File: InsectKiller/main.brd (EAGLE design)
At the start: 28 parts, among them IC3 NE555N, Q1 BCF29SMD, Q2 IRF530, Q3 BCX71SMD

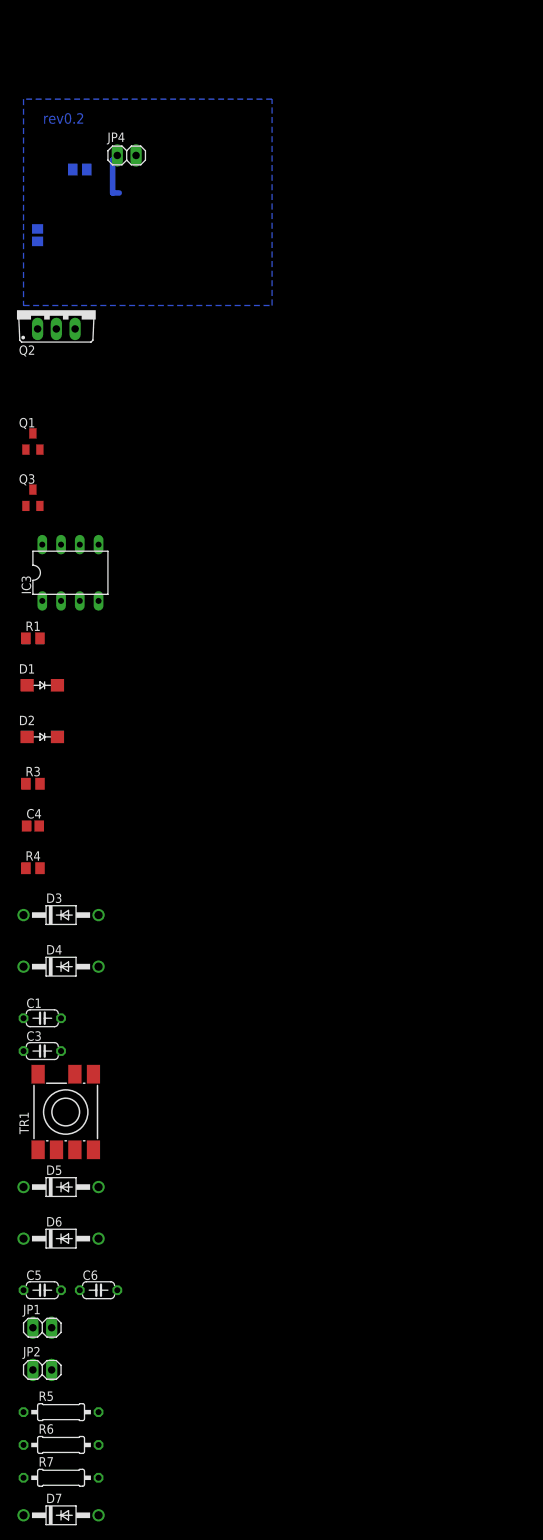
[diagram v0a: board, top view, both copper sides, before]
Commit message: Fixed element values.
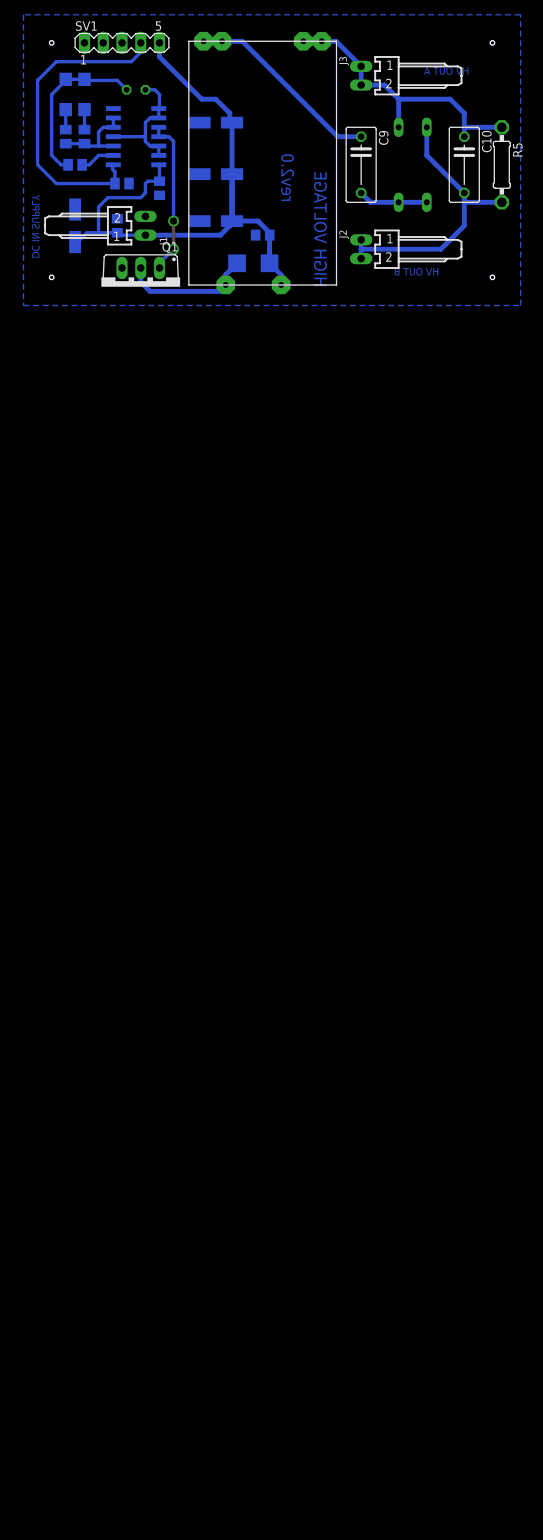
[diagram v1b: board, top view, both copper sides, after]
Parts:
- removed D6, D7: 1N4004, diode:DO41-10
- removed IC3: NE555N, linear:DIL08
- removed JP1, JP2, JP4: (no value), pinhead:1X02
- removed Q2: IRF530, transistor-power:TO220BV
- removed Q3: BCX71SMD, transistor-pnp:SOT23
- removed R6, R7: (no value), resistor:0207/10
- removed TR1: (no value), inductor-neosid:SM-R6
- added 11: CCFL_INVERTER_COIL, ccfl_inverter_coil:CCFL_INVERTER_COIL
- added C10: 2n2/4k, resistor:C075-042X103
- added C7, C8: 220n, resistor:C0805
- added C9: 2n2/4k, rcl:C075-042X103
- added IC1: 4011D, 40xx:SO14
- added J1, J2, J3: 22-05-7028-02, con-molex:7395-02
- added SV1: (no value), con-lstb:MA05-1
- C1: value (none) -> 47n; device resistor:C050-024X044 -> resistor:C025-025X050
- C2: value 220n -> 100n
- C3, C6: value (none) -> 100u/16V; device resistor:C050-024X044 -> rcl:153CLV-0505
- C4: value 220n -> 100u/16V; device resistor:C0805 -> rcl:153CLV-0505
- C5: value (none) -> 100u/16V; device resistor:C050-024X044 -> resistor:153CLV-0505
- D3: value 1N4004 -> ES2D; device diode:DO41-10 -> diode:SMB
- D4, D5: value 1N4004 -> BAV21; device diode:DO41-10 -> diode:DO35-10
- Q1: value BCF29SMD -> IRF530; device transistor-npn:SOT23-BEC -> transistor-power:TO220BV
- R1: value 2k2 -> 4k7
- R2: value 2k2 -> 22k
- R3: value 2k2 -> 5k1
- R4: value 2k2 -> 330R
- R5: value (none) -> 33M
- moved R5 179.1 mm to (64.8, 19.1), turned to 270 degrees
- moved C6 158.9 mm to (26.0, 24.8), flipped to the bottom, turned to 180 degrees
- moved C5 152.9 mm to (26.0, 17.8), flipped to the bottom, turned to 180 degrees
- moved D5 147.0 mm to (54.6, 19.1), flipped to the bottom, turned to 270 degrees
- moved C1 126.4 mm to (15.2, 29.2), flipped to the bottom
- moved D4 117.8 mm to (50.8, 19.1), flipped to the bottom, turned to 90 degrees
- moved C3 111.8 mm to (6.99, 10.8), flipped to the bottom, turned to 270 degrees
- moved R4 99.3 mm to (8.26, 22.9), flipped to the bottom, turned to 90 degrees
- moved D3 92.0 mm to (31.1, 5.71), flipped to the bottom
- moved R3 87.7 mm to (5.71, 22.9), flipped to the bottom, turned to 90 degrees
- moved D2 87.2 mm to (8.26, 28.6), flipped to the bottom, turned to 90 degrees
- moved C4 85.6 mm to (26.0, 11.4), flipped to the bottom, turned to 180 degrees
- moved D1 80.1 mm to (5.71, 28.6), flipped to the bottom, turned to 270 degrees
- moved R1 62.8 mm to (13.3, 16.5), flipped to the bottom
- moved Q1 25.5 mm to (15.9, 2.54), turned to 180 degrees
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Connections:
- removed net N$12: C1.2, C5.1, D3.C, D4.A
- removed net N$13: R5.2, R6.1
- removed net N$14: C3.2, C6.1, D4.C, D5.A
- removed net N$15: C5.2, D5.C, D6.A
- removed net N$16: C6.2, D6.C, JP1.1, JP1.2
- removed net N$17: JP2.1, JP2.2, R7.2
- removed net N$18: R6.2, R7.1
- removed net N$8: C2.1, D1.A, D2.K, IC3.2, IC3.6
- new net N$22: IC1.3, IC1.5, IC1.6, R3.1, R4.1
- new net N$23: C1.2, D1.A, D2.K, R2.2
- new net N$25: D2.A, R4.2
- net GND: now also C3.-, C4.-, C5.-, C6.-, C7.2, C8.2, IC1.7, J1.2, Q1.S, SV1.1, SV1.2, SV1.3; no longer C4.2, IC3.1, JP4.2, Q2.S, Q3.3
- net N$1: now also IC1.2, R2.1; no longer Q1.E, Q3.2, R2.2
- net N$10: now also C10.2, D5.C, J2.1, J2.2, R5.2; no longer D2.A, R1.2
- net N$11: now also 11.S2.A, 11.S2.B, C10.1, D4.A, J3.1, J3.2; no longer C3.1, D3.A, TR1.5
- net N$2: now also IC1.1, R1.2, SV1.4; no longer Q2.G, R2.1
- net N$3: now also 11.P2, D3.A, Q1.D; no longer D7.A, Q2.D, TR1.4
- net N$4: now also IC1.10, IC1.11, Q1.G; no longer IC3.7, Q1.B, Q3.1, R4.2
- net N$5: now also C1.1, IC1.12, IC1.13, IC1.4, IC1.8, IC1.9; no longer IC3.3, R1.1, R3.1
- net N$6: now also 11.S1.A, 11.S1.B, C9.1; no longer C4.1, IC3.5
- net N$7: now also C9.2, D4.C, D5.A; no longer C1.1, TR1.8
- net VCC: now also 11.P1, C2.1, C3.+, C4.+, C5.+, C6.+, C7.1, C8.1, D3.C, IC1.14, J1.1, R1.1, SV1.5; no longer D7.C, IC3.4, IC3.8, JP4.1, Q1.C, R4.1, TR1.1
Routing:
- net VCC: track 6.23 -> 88.8 mm
- net N$2: track 0.00 -> 42.5 mm
- net N$10: track 0.00 -> 39.6 mm
- net N$11: track 0.00 -> 39.4 mm
- net N$6: track 0.00 -> 26.7 mm
- net N$23: track 0.00 -> 22.7 mm
- net N$4: track 0.00 -> 21.5 mm, vias 0 -> 2
- net N$3: track 0.00 -> 18.2 mm
- net N$5: track 0.00 -> 17.7 mm
- net N$22: track 0.00 -> 12.0 mm
- net N$7: track 0.00 -> 9.42 mm
- net N$1: track 0.00 -> 4.76 mm
- net N$25: track 0.00 -> 2.71 mm
- net N$24: track 0.00 -> 2.71 mm
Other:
- board text added: "DC IN SUPPLY"
- board text added: "HIGH VOLTAGE"
- board text added: "HV OUT A"
- board text added: "HV OUT B"
- board text added: "rev2.0"
- board text removed: "rev0.2"

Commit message: Fixed capacitor value.
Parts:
- C10, C9: value 2n2/4k -> 4n7/4k
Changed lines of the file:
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@@
 <element name="C7" library="resistor" package="C0805" value="220n" x="18.415" y="15.875" rot="MR270"/>
 <element name="Q1" library="transistor-power" package="TO220BV" value="IRF530" x="15.875" y="2.54" rot="R180"/>
-<element name="C9" library="rcl" package="C075-042X103" value="2n2/4k" x="45.72" y="19.05" rot="R270"/>
+<element name="C9" library="rcl" package="C075-042X103" value="4n7/4k" x="45.72" y="19.05" rot="R270"/>
 <element name="R5" library="resistor" package="0207/10" value="33M" x="64.77" y="19.05" rot="R270"/>
 <element name="D3" library="diode" package="SMB" value="ES2D" x="31.115" y="5.715" rot="MR0"/>
@@
 <element name="C8" library="resistor" package="C0805" value="220n" x="32.385" y="9.525" rot="MR0"/>
 <element name="D5" library="diode" package="DO35-10" value="BAV21" x="54.61" y="19.05" rot="MR270"/>
-<element name="C10" library="resistor" package="C075-042X103" value="2n2/4k" x="59.69" y="19.05" rot="R270"/>
+<element name="C10" library="resistor" package="C075-042X103" value="4n7/4k" x="59.69" y="19.05" rot="R270"/>
 <element name="D4" library="diode" package="DO35-10" value="BAV21" x="50.8" y="19.05" rot="MR90"/>
 <element name="C2" library="resistor" package="C0805" value="100n" x="12.7" y="10.795" rot="MR90"/>
